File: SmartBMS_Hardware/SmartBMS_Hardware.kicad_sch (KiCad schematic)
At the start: 1 part, among them T1 Transformer_1P_1S

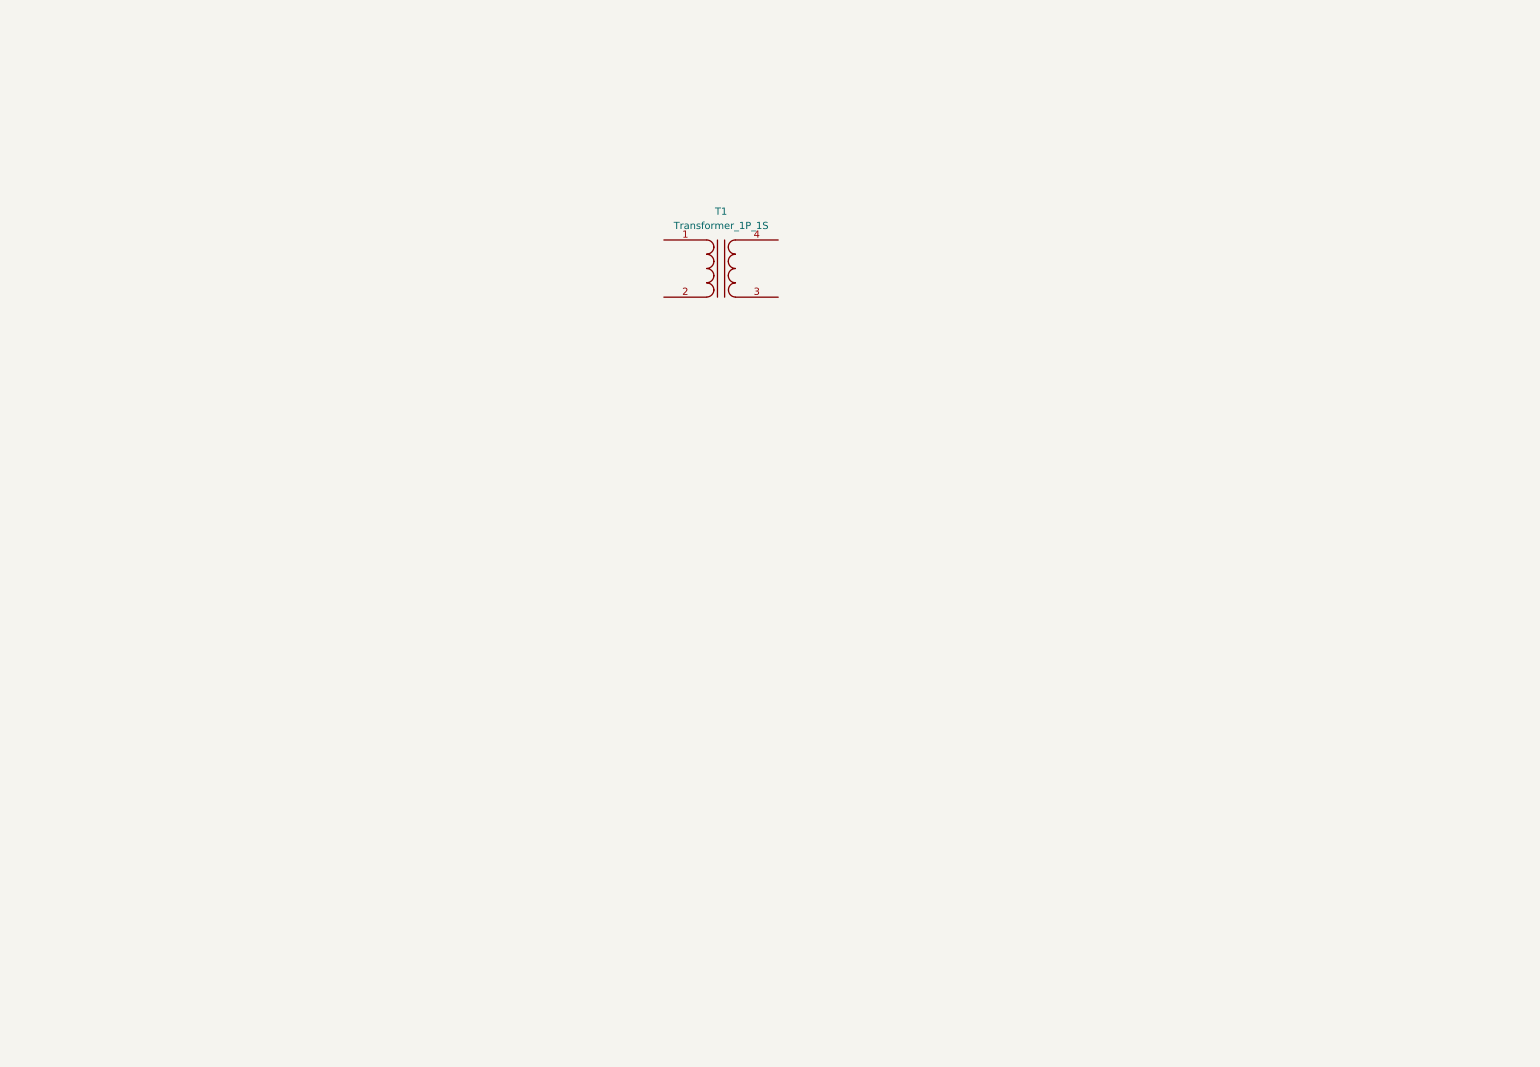
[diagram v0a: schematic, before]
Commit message: Added Flyback and Teensy
Added the flyback transformer circuit and made a teensy with the labels corresponding to the flyback transformer switches.
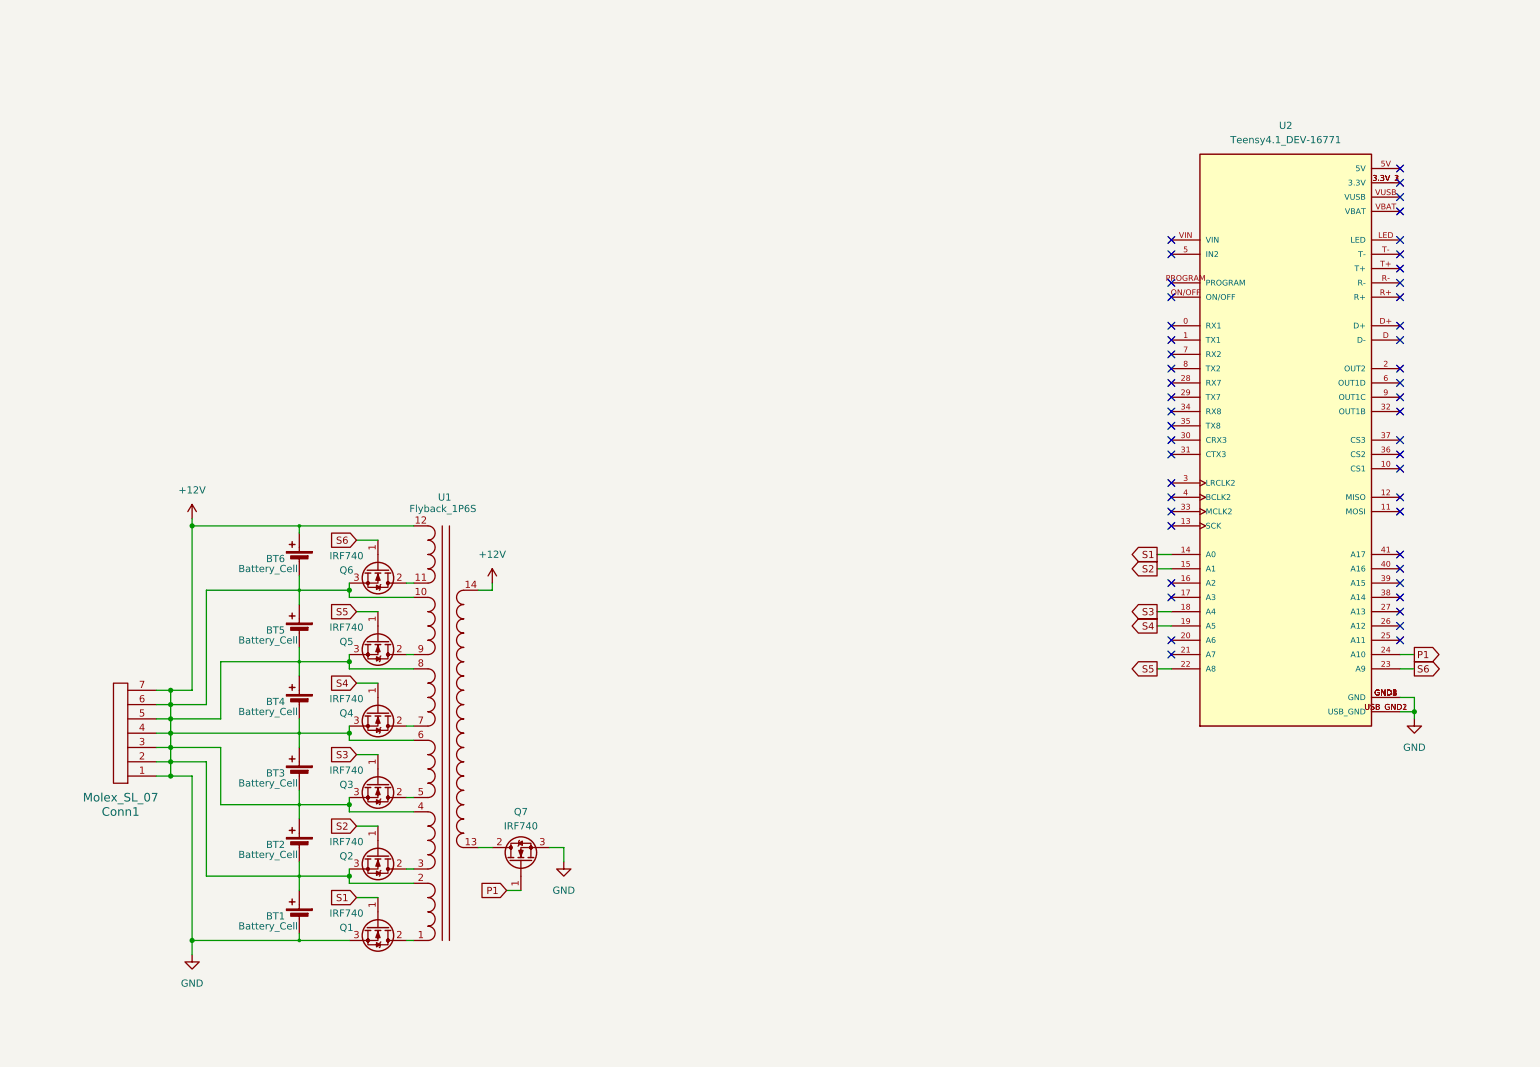
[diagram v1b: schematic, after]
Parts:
- removed T1: Transformer_1P_1S, symbol Device:Transformer_1P_1S
- added BT1, BT2, BT3, BT4, BT5, BT6: Battery_Cell, symbol Device:Battery_Cell
- added Conn1: Molex_SL_07, symbol MRDT_Connectors:Molex_SL_07
- added Q1, Q2, Q3, Q4, Q5, Q6, Q7: IRF740, Package_TO_SOT_THT:TO-220-3_Vertical, symbol Transistor_FET:IRF740
- added U1: Flyback_1P6S, symbol Symbols:Flyback_1p6s
- added U2: Teensy4.1_DEV-16771, MODULE_DEV-16771, symbol MRDT_Shields:Teensy4.1_DEV-16771
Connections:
- new net: Q1.2 (D), U1.1
- new net: Q6.2 (D), U1.11
- new net: Q7.2 (D), U1.13
- new net: Q2.2 (D), U1.3
- new net: Q3.2 (D), U1.5
- new net: Q4.2 (D), U1.7
- new net: Q5.2 (D), U1.9
- new net: U2.3.3V_1 (3.3V), U2.3.3V_2 (3.3V), U2.3.3V_3 (3.3V)
- new net +12V: BT1.1 (+), BT1.2 (-), BT2.1 (+), BT2.2 (-), BT3.1 (+), BT3.2 (-), BT4.1 (+), BT4.2 (-), BT5.1 (+), BT5.2 (-), BT6.1 (+), BT6.2 (-), Conn1.1, Conn1.2, Conn1.3, Conn1.4, Conn1.5, Conn1.6, Conn1.7, Q1.3 (S), Q2.3 (S), Q3.3 (S), Q4.3 (S), Q5.3 (S), Q6.3 (S), Q7.3 (S), U1.10, U1.12, U1.14, U1.2, U1.4, U1.6, U1.8, U2.GND1 (GND), U2.GND2 (GND), U2.GND3 (GND), U2.GND4 (GND), U2.GND5 (GND), U2.USB_GND1 (USB_GND), U2.USB_GND2 (USB_GND)
- new net P1: Q7.1 (G), U2.24 (A10)
- new net S1: Q1.1 (G), U2.14 (A0)
- new net S2: Q2.1 (G), U2.15 (A1)
- new net S3: Q3.1 (G), U2.18 (A4)
- new net S4: Q4.1 (G), U2.19 (A5)
- new net S5: Q5.1 (G), U2.22 (A8)
- new net S6: Q6.1 (G), U2.23 (A9)
- no-connect marks 0 -> 49

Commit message: Fixed an issue with Flyback transformer
Removed wires connecting the connector pins together in the flyback transformer circuit
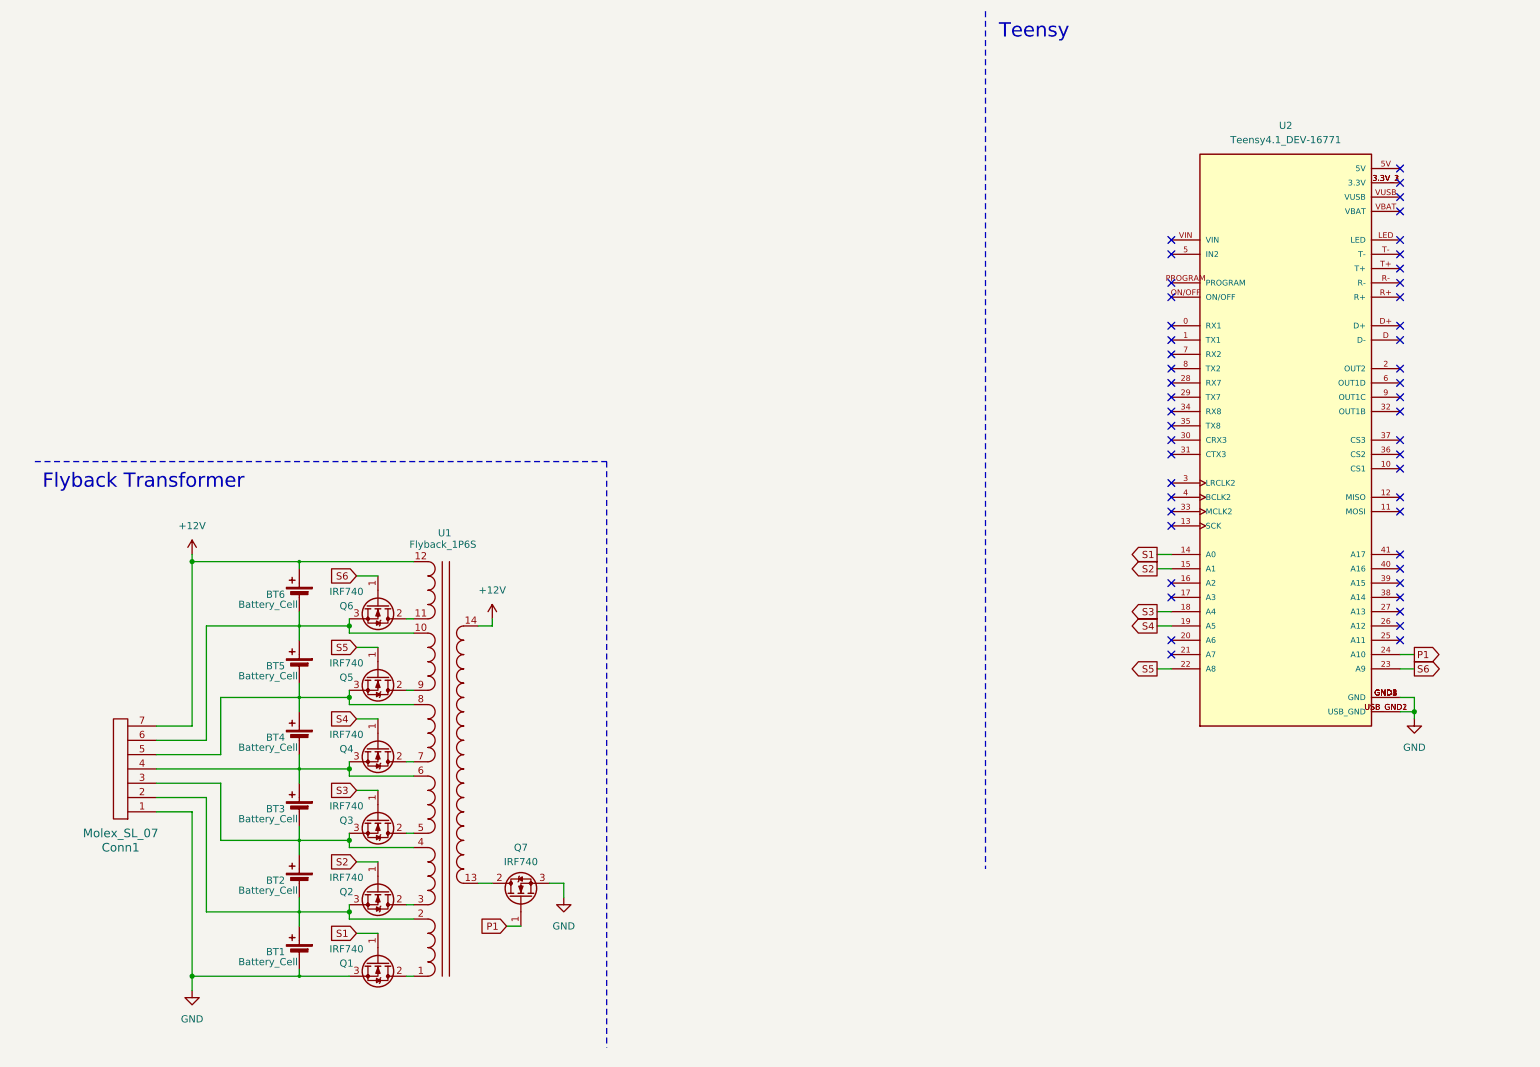
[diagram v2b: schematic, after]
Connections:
- net +12V: no longer BT1.1 (+), BT1.2 (-), BT2.1 (+), BT2.2 (-), BT3.1 (+), BT3.2 (-), BT4.1 (+), BT4.2 (-), BT5.1 (+), BT5.2 (-), BT6.2 (-), Conn1.1, Conn1.2, Conn1.3, Conn1.4, Conn1.5, Conn1.6, Q1.3 (S), Q2.3 (S), Q3.3 (S), Q4.3 (S), Q5.3 (S), Q6.3 (S), Q7.3 (S), U1.10, U1.2, U1.4, U1.6, U1.8, U2.GND1 (GND), U2.GND2 (GND), U2.GND3 (GND), U2.GND4 (GND), U2.GND5 (GND), U2.USB_GND1 (USB_GND), U2.USB_GND2 (USB_GND)
- new net: BT5.1 (+), BT6.2 (-), Conn1.6, Q6.3 (S), U1.10
- new net: BT1.1 (+), BT2.2 (-), Conn1.2, Q2.3 (S), U1.2
- new net: BT2.1 (+), BT3.2 (-), Conn1.3, Q3.3 (S), U1.4
- new net: BT3.1 (+), BT4.2 (-), Conn1.4, Q4.3 (S), U1.6
- new net: BT4.1 (+), BT5.2 (-), Conn1.5, Q5.3 (S), U1.8
- new net GND: BT1.2 (-), Conn1.1, Q1.3 (S), Q7.3 (S), U2.GND1 (GND), U2.GND2 (GND), U2.GND3 (GND), U2.GND4 (GND), U2.GND5 (GND), U2.USB_GND1 (USB_GND), U2.USB_GND2 (USB_GND)
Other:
- note added: "Flyback Transformer"
- note added: "Teensy"
- moved on the sheet: BT1, BT2, BT3, BT4, BT5, BT6, Conn1, Q1, Q2, Q3, Q4, Q5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

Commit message: Added cell sensing
Added cell sensing op amps from PMS hardware, added current sensing from PMS hardware.
Current sensing may or may not be needed, however I added it just in case since the PMS had a current sensing input included in the cell sensing circuit.
Teensy was also updated with the necessary inputs and outputs for the additional circuits.
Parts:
- added Conn2: Molex_SL_07, MRDT_Connectors:MOLEX_SL_07_Horizontal, symbol MRDT_Connectors:Molex_SL_07
- added R1, R12, R13, R16, R17, R20, R21, R24, R4, R5, R8, R9: 36.5k, Resistor_SMD:R_0603_1608Metric_Pad0.98x0.95mm_HandSolder, symbol Device:R
- added R10, R11, R14, R15, R18, R19, R2, R22, R23, R3, R6, R7: 46.4k, Resistor_SMD:R_0603_1608Metric_Pad0.98x0.95mm_HandSolder, symbol Device:R
- added U3, U4, U5: Opamp_Dual, Package_SO:SO-8_3.9x4.9mm_P1.27mm, symbol Device:Opamp_Dual
- added U6: ACS758xCB-200B-PFF, Sensor_Current:Allegro_CB_PFF, symbol Sensor_Current:ACS758xCB-200B-PFF
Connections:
- net GND: now also Conn2.1, R1.1, R13.1, R17.1, R21.1, R23.1, R5.1, R9.1, U3.4 (V-), U4.4 (V-), U5.4 (V-), U6.2 (GND)
- net P1: now also U2.25 (A11); no longer U2.24 (A10)
- net S1: now also U2.3 (LRCLK2); no longer U2.14 (A0)
- net S2: now also U2.4 (BCLK2); no longer U2.15 (A1)
- net S3: now also U2.33 (MCLK2); no longer U2.18 (A4)
- net S4: now also U2.13 (SCK); no longer U2.19 (A5)
- net Cell4-SENSE: now reaches U2.16 (A2)
- net Cell4-SENSE: now also U2.17 (A3), R12.2, U4.7
- new net: R17.2, R18.2, U5.5 (+)
- new net: R1.2, R2.2, U3.5 (+)
- new net: R7.2, R8.1, U3.2 (-)
- new net: R10.2, R9.2, U4.5 (+)
- new net: R3.2, R4.1, U3.6 (-)
- new net: R5.2, R6.2, U3.3 (+)
- new net: R15.2, R16.1, U4.2 (-)
- new net: R19.2, R20.1, U5.6 (-)
- new net: R13.2, R14.2, U4.3 (+)
- new net: R11.2, R12.1, U4.6 (-)
- new net: R23.2, R24.1, U5.2 (-)
- new net: R21.2, R22.2, U5.3 (+)
- new net +3.3V: U6.1 (VCC)
- new net +BATT: U6.5 (IP-)
- new net CURRENT_SENSE: U2.24 (A10), U6.3 (VIOUT)
- new net Cell1-SENSE: R24.2, U2.18 (A4), U5.1
- new net Cell2-SENSE: R20.2, U2.19 (A5), U5.7
- new net Cell3-SENSE: R16.2, U2.15 (A1), U4.1
- new net Cell5-SENSE: R8.2, U2.14 (A0), U3.1
- new net Cell6-SENSE: R4.2, U3.7
- new net PV: U3.8 (V+), U4.8 (V+), U5.8 (V+), U6.4 (IP+)
- new net cell1: Conn2.2, R19.1, R22.1
- new net cell2: Conn2.3, R15.1, R18.1
- new net cell3: Conn2.4, R11.1, R14.1
- new net cell4: Conn2.5, R10.1, R7.1
- new net cell5: Conn2.6, R3.1, R6.1
- new net cell6: Conn2.7, R2.1
- no-connect marks 49 -> 42
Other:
- note added: "Cell Sensor Op Amps"
- note added: "Connectors"
- note added: "Current Sensing"
